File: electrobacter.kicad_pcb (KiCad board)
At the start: 2 copper layers, 123 x 139.7 mm, 58 parts, among them J1 CONN_switch, J2 CONN_Bateria, J3 CONN_programador, J4 Conn_01x04_Male, J5 CONN_botones, J6 CONN_OUT, J7 conn_reset, J8 conn_reset, Q1 BC547, Q2 BC327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

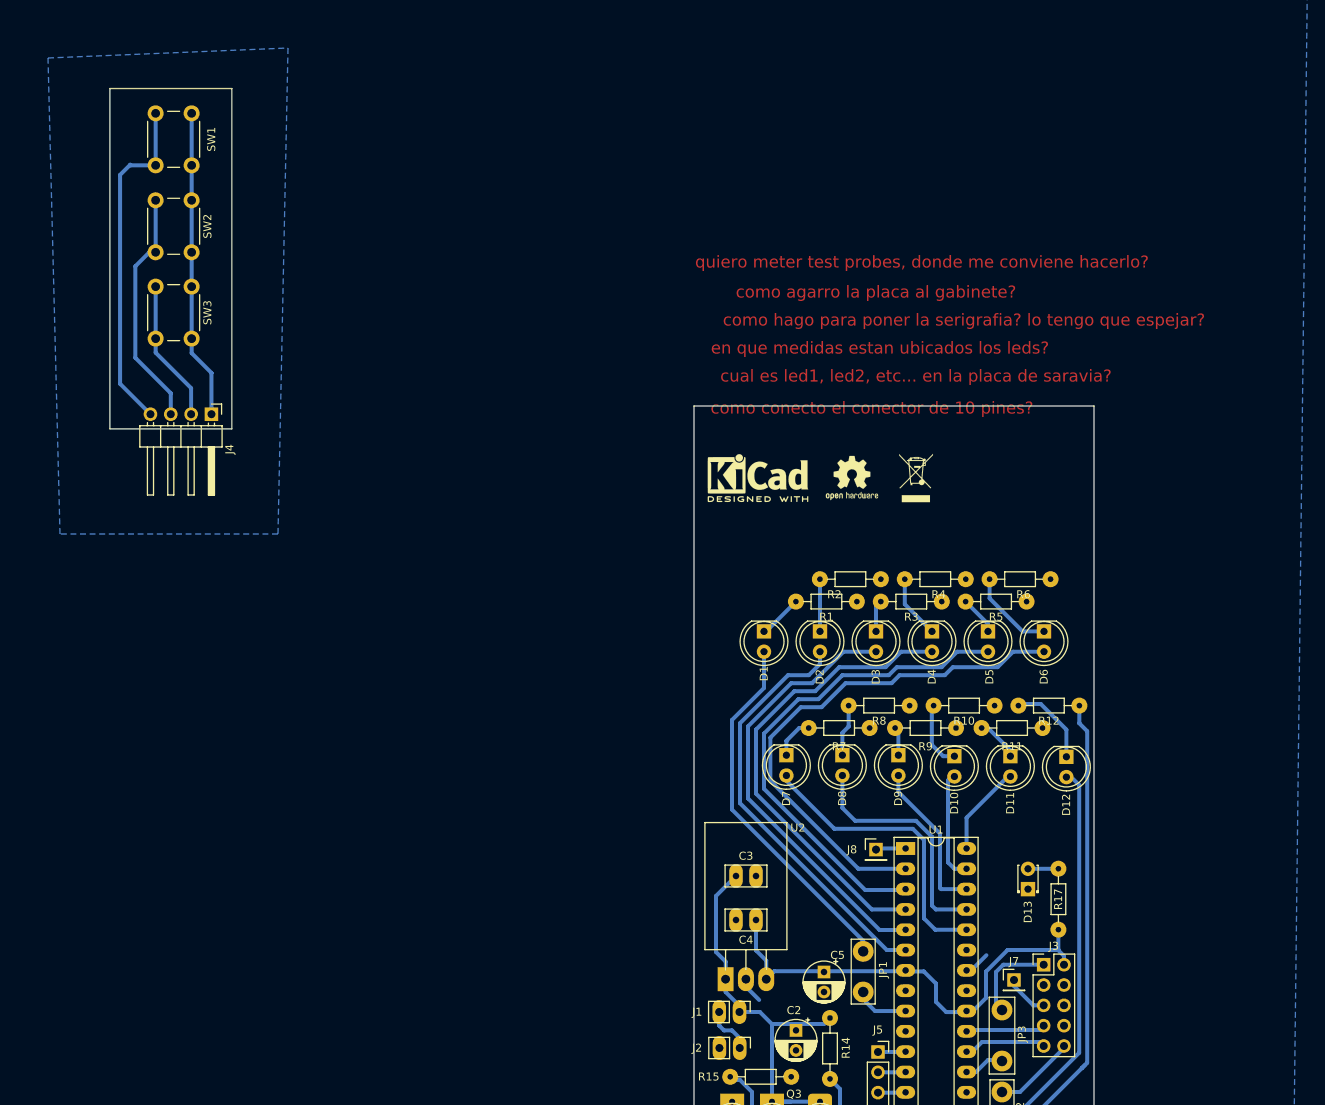
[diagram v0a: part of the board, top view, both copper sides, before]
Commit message: añadidos pdfs y hechos pequeños cambios esteticos en la placa
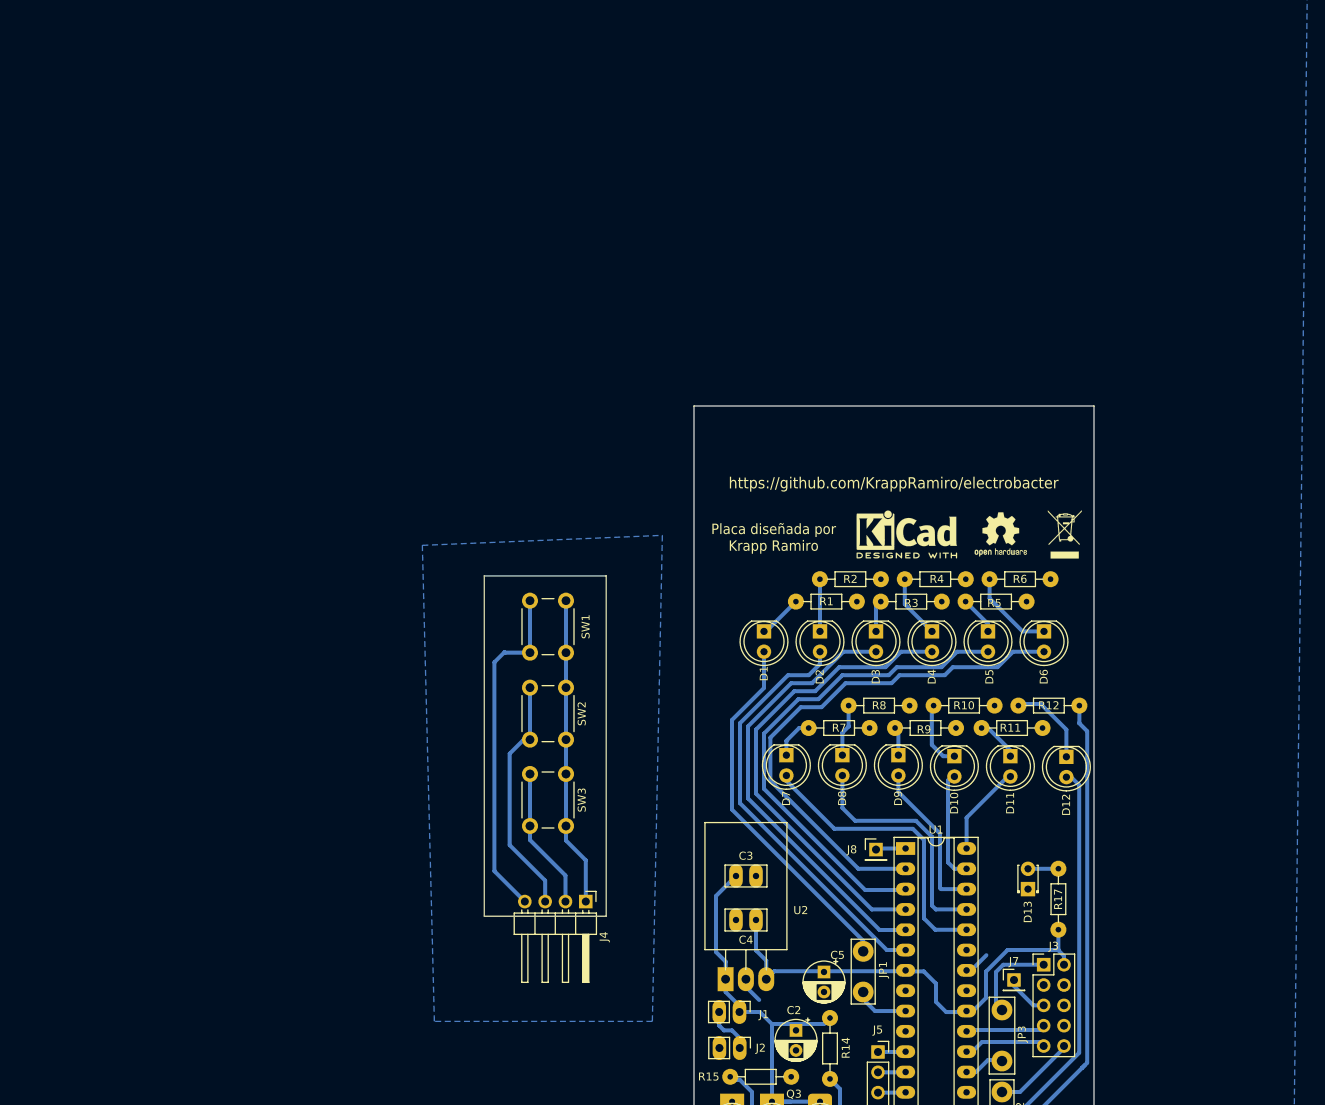
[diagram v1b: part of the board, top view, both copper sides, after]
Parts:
- moved SW2 76.8 mm to (199.2, 87.0)
- moved SW3 76.8 mm to (199.2, 97.8)
- moved J4 76.8 mm to (201.7, 113.7)
- moved SW1 76.8 mm to (199.2, 76.1)
- moved REF** 19.9 mm to (261.6, 67.8)
- moved REF** 19.9 mm to (253.6, 67.8)
- moved REF** 19.9 mm to (241.8, 67.8)
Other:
- board size 123 x 139.7 mm -> 76.2 x 100 mm
- board text added: "Placa diseñada por Krapp Ramiro"
- board text added: "https://github.com/KrappRamiro/electrobacter"
- board text removed: "como agarro la placa al gabinete?"
- board text removed: "como conecto el conector de 10 pines?"
- board text removed: "como hago para poner la serigrafia? lo tengo que espejar?"
- board text removed: "cual es led1, led2, etc... en la placa de saravia?"
- board text removed: "en que medidas estan ubicados los leds?"
- board text removed: "quiero meter test probes, donde me conviene hacerlo?"
